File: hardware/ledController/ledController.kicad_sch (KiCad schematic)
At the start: 15 parts, among them IC1 PIC16F1769-I_ML, J1 Conn_01x06, J2 Screw_Terminal_01x02, J3 Screw_Terminal_01x02, J4 Conn_01x06, J5 Conn_01x03

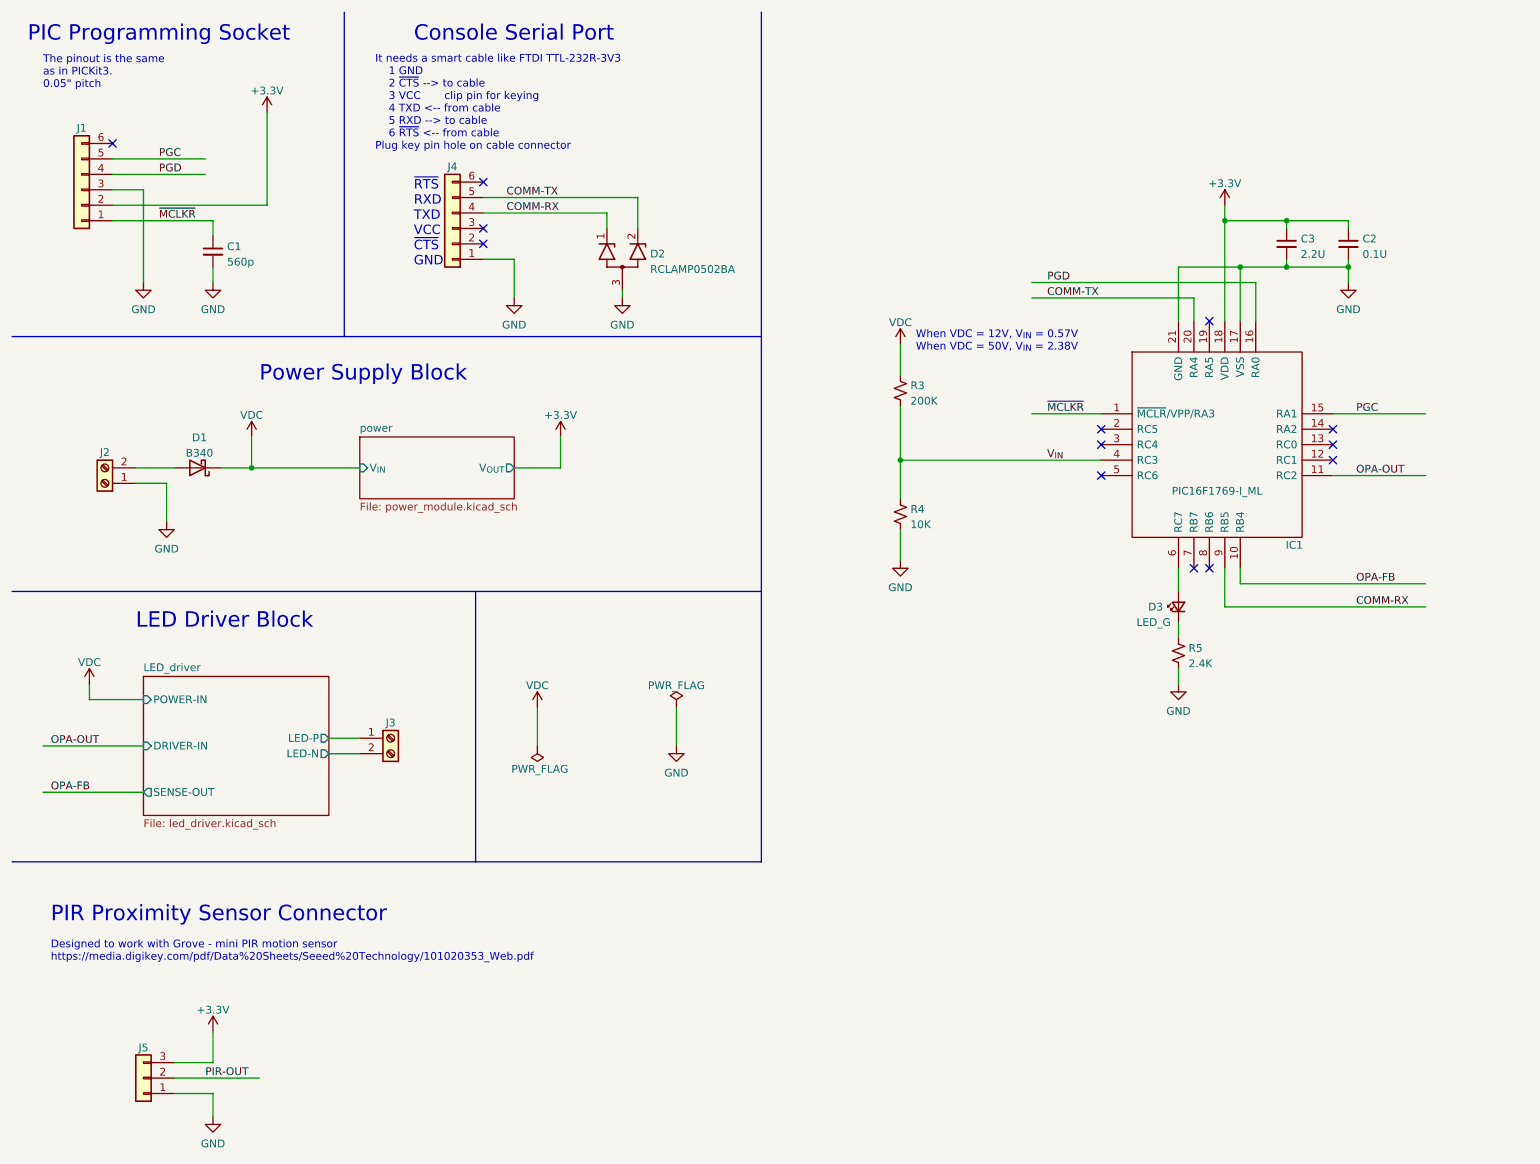
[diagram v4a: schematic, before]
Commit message: More schematic updates
Moved from PIR sensor to photoresistor + additional components
Added mounting holes
Moved to a stand alone 3.3V switcher
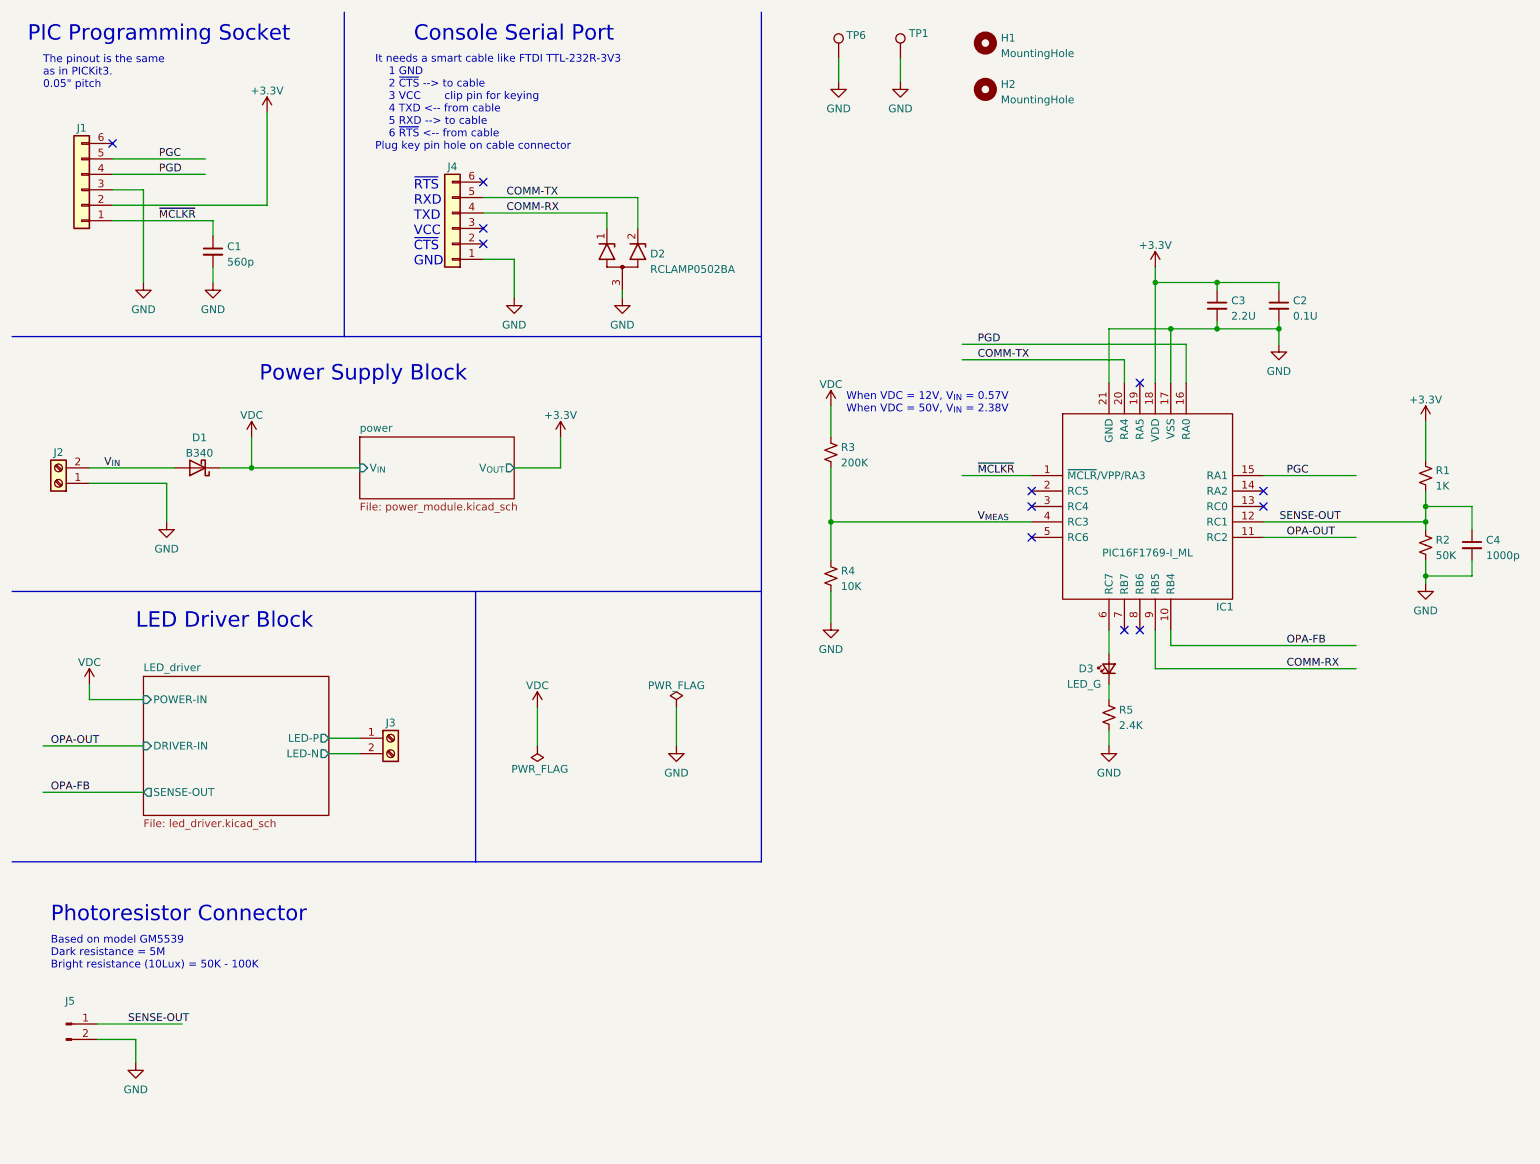
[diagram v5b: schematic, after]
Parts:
- removed J5: Conn_01x03, molex-footprints:353620350, symbol Connector_Generic:Conn_01x03
- added C4: 1000p, Capacitor_SMD:C_0402_1005Metric_Pad0.74x0.62mm_HandSolder, symbol Device:C_Small
- added H1, H2: MountingHole, MountingHole:MountingHole_2.5mm_Pad_TopBottom, symbol Mechanical:MountingHole
- added J5: Conn_01x02_Male, Connector_PinSocket_2.54mm:PinSocket_1x02_P2.54mm_Vertical, symbol Connector:Conn_01x02_Male
- added R1: 1K, Resistor_SMD:R_0603_1608Metric_Pad0.98x0.95mm_HandSolder, symbol Device:R_Small_US
- added R2: 50K, Resistor_SMD:R_0603_1608Metric_Pad0.98x0.95mm_HandSolder, symbol Device:R_Small_US
- added TP1, TP6: TestPoint, ym-footprints:TestPoint_Pad_0.185in_x_0.135in, symbol Connector:TestPoint
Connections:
- net +3.3V: now also R1.1
- net GND: now also C4.2, J5.2 (Pin_2), R2.2, TP1.1, TP6.1
- net V_{IN}: now also D1.2 (A), J2.2 (Pin_2); no longer IC1.4 (RC3), R3.2, R4.1
- net SENSE-OUT: now reaches IC1.12 (RC1)
- net SENSE-OUT: now also C4.1, J5.1 (Pin_1), R1.2, R2.1
- new net V_{MEAS}: IC1.4 (RC3), R3.2, R4.1
- no-connect marks 13 -> 12
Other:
- note added: "Based on model GM5539 Dark resistance = 5M Bright resistance (10Lux) = 50K - 100K"
- note added: "Photoresistor Connector"
- note removed: "Designed to work with Grove - mini PIR motion sensor https://media.digikey.com/pdf/Data%20Sheets/Seeed%20Technology/101020353_Web.pdf"
- note removed: "PIR Proximity Sensor Connector"
- moved on the sheet: C2, C3, D3, IC1, J2, R3, R4, R5

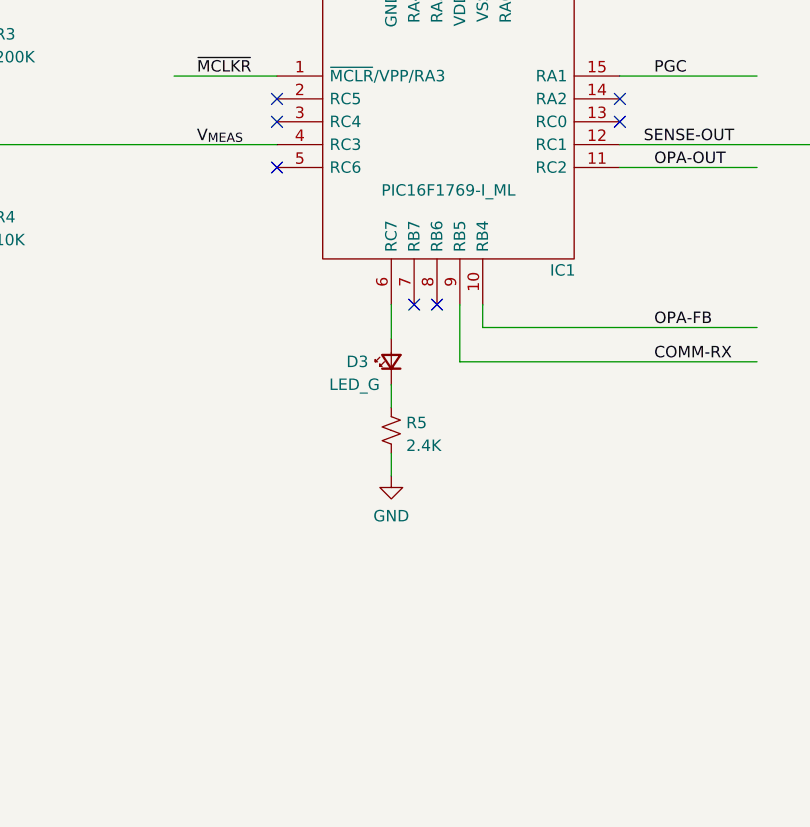
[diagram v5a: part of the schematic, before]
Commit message: Replaced debug LED
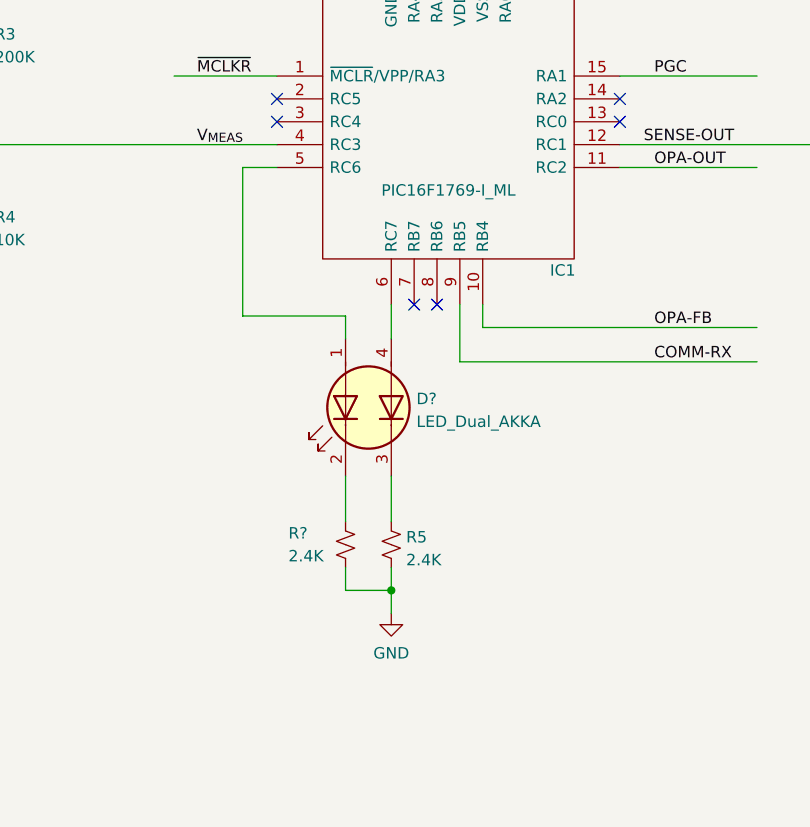
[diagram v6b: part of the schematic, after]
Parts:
- removed D3: LED_G, LED_SMD:LED_0805_2012Metric_Pad1.15x1.40mm_HandSolder, symbol Device:LED_Small
- added D?: LED_Dual_AKKA, LED_SMD:LED_Kingbright_APHBM2012_2x1.25mm, symbol Device:LED_Dual_AKKA
- added R?: 2.4K, Resistor_SMD:R_0603_1608Metric_Pad0.98x0.95mm_HandSolder, symbol Device:R_Small_US
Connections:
- net GND: now also R?.2
- net at IC1.5 (RC6): now also D?.1 (A1)
- net at IC1.6 (RC7): now also D?.4 (A2)
- net at R5.1: now also D?.3 (K2)
- new net: D?.2 (K1), R?.1
- no-connect marks 12 -> 11
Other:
- moved on the sheet: R5
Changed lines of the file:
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@@
   (junction (at 200.66 57.15) (diameter 0) (color 0 0 0 0)
+  )
+  (junction (at 193.04 146.05) (diameter 0) (color 0 0 0 0)
   )
   (junction (at 147.32 96.52) (diameter 0) (color 0 0 0 0)
@@
   (no_connect (at 90.17 48.26))
   (no_connect (at 90.17 40.64))
-  (no_connect (at 180.34 99.06))
   (no_connect (at 180.34 93.98))
   (no_connect (at 195.58 114.3))
@@
     (stroke (width 0) (type default) (color 0 0 0 0))
   )
+  (wire (pts (xy 193.04 114.3) (xy 193.04 118.11))
+    (stroke (width 0) (type default) (color 0 0 0 0))
+  )
   (wire (pts (xy 102.87 87.63) (xy 102.87 82.55))
     (stroke (width 0) (type default) (color 0 0 0 0))
@@
     (stroke (width 0) (type default) (color 0 0 0 0))
   )
+  (wire (pts (xy 176.53 99.06) (xy 176.53 115.57))
+    (stroke (width 0) (type default) (color 0 0 0 0))
+  )
   (wire (pts (xy 218.44 88.9) (xy 233.68 88.9))
     (stroke (width 0) (type default) (color 0 0 0 0))
   )
-  (wire (pts (xy 193.04 123.19) (xy 193.04 125.73))
-    (stroke (width 0) (type default) (color 0 0 0 0))
-  )
   (wire (pts (xy 52.07 87.63) (xy 69.85 87.63))
     (stroke (width 0) (type default) (color 0 0 0 0))
@@
     (stroke (width 0) (type default) (color 0 0 0 0))
   )
+  (wire (pts (xy 187.96 115.57) (xy 187.96 118.11))
+    (stroke (width 0) (type default) (color 0 0 0 0))
+  )
   (wire (pts (xy 218.44 96.52) (xy 245.11 96.52))
     (stroke (width 0) (type default) (color 0 0 0 0))
@@
     (stroke (width 0) (type default) (color 0 0 0 0))
   )
+  (wire (pts (xy 193.04 146.05) (xy 193.04 148.59))
+    (stroke (width 0) (type default) (color 0 0 0 0))
+  )
   (wire (pts (xy 90.17 53.34) (xy 95.25 53.34))
     (stroke (width 0) (type default) (color 0 0 0 0))
@@
     (stroke (width 0) (type default) (color 0 0 0 0))
   )
+  (wire (pts (xy 180.34 99.06) (xy 176.53 99.06))
+    (stroke (width 0) (type default) (color 0 0 0 0))
+  )
   (wire (pts (xy 245.11 93.98) (xy 252.73 93.98))
     (stroke (width 0) (type default) (color 0 0 0 0))
@@
     (stroke (width 0) (type default) (color 0 0 0 0))
   )
+  (wire (pts (xy 187.96 133.35) (xy 187.96 138.43))
+    (stroke (width 0) (type default) (color 0 0 0 0))
+  )
   (wire (pts (xy 25.4 90.17) (xy 38.1 90.17))
     (stroke (width 0) (type default) (color 0 0 0 0))
@@
     (stroke (width 0) (type default) (color 0 0 0 0))
   )
+  (wire (pts (xy 193.04 133.35) (xy 193.04 138.43))
+    (stroke (width 0) (type default) (color 0 0 0 0))
+  )
   (wire (pts (xy 245.11 96.52) (xy 245.11 97.79))
     (stroke (width 0) (type default) (color 0 0 0 0))
   )
+  (wire (pts (xy 187.96 143.51) (xy 187.96 146.05))
+    (stroke (width 0) (type default) (color 0 0 0 0))
+  )
   (wire (pts (xy 252.73 105.41) (xy 245.11 105.41))
     (stroke (width 0) (type default) (color 0 0 0 0))
@@
     (stroke (width 0) (type default) (color 0 0 0 0))
   )
-  (wire (pts (xy 193.04 130.81) (xy 193.04 133.35))
+  (wire (pts (xy 193.04 143.51) (xy 193.04 146.05))
     (stroke (width 0) (type default) (color 0 0 0 0))
   )
@@
     (stroke (width 0) (type default) (color 0 0 0 0))
   )
-  (wire (pts (xy 193.04 114.3) (xy 193.04 118.11))
-    (stroke (width 0) (type default) (color 0 0 0 0))
-  )
   (wire (pts (xy 252.73 102.87) (xy 252.73 105.41))
     (stroke (width 0) (type default) (color 0 0 0 0))
@@
     (stroke (width 0) (type default) (color 0 0 0 0))
   )
+  (wire (pts (xy 176.53 115.57) (xy 187.96 115.57))
+    (stroke (width 0) (type default) (color 0 0 0 0))
+  )
   (wire (pts (xy 95.25 87.63) (xy 102.87 87.63))
     (stroke (width 0) (type default) (color 0 0 0 0))
@@
   )
   (wire (pts (xy 26.67 181.61) (xy 33.02 181.61))
+    (stroke (width 0) (type default) (color 0 0 0 0))
+  )
+  (wire (pts (xy 187.96 146.05) (xy 193.04 146.05))
     (stroke (width 0) (type default) (color 0 0 0 0))
   )
@@
     (pin "2")
   )
+  (symbol (lib_id "Device:R_Small_US") (at 187.96 140.97 0) (unit 1)
+    (in_bom yes) (on_board yes)
+    (property "Reference" "R?" (id 0) (at 181.61 139.7 0)
+      (effects (font (size 1.27 1.27)) (justify left))
+    )
+    (property "Value" "2.4K" (id 1) (at 181.61 142.24 0)
+      (effects (font (size 1.27 1.27)) (justify left))
+    )
+    (property "Footprint" "Resistor_SMD:R_0603_1608Metric_Pad0.98x0.95mm_HandSolder" (id 2) (at 187.96 140.97 0)
+      (effects (font (size 1.27 1.27)) hide)
+    )
+    (property "Datasheet" "~" (id 3) (at 187.96 140.97 0)
+      (effects (font (size 1.27 1.27)) hide)
+    )
+    (pin "1")
+    (pin "2")
+  )
   (symbol (lib_id "power:GND") (at 220.98 67.31 0) (unit 1)
     (in_bom yes) (on_board yes) (fields_autoplaced)
@@
     (pin "1")
     (pin "2")
+  )
+  (symbol (lib_id "Device:LED_Dual_AKKA") (at 190.5 125.73 90) (mirror x) (unit 1)
+    (in_bom yes) (on_board yes) (fields_autoplaced)
+    (property "Reference" "D?" (id 0) (at 195.834 124.7683 90)
+      (effects (font (size 1.27 1.27)) (justify right))
+    )
+    (property "Value" "LED_Dual_AKKA" (id 1) (at 195.834 127.3052 90)
+      (effects (font (size 1.27 1.27)) (justify right))
+    )
+    (property "Footprint" "LED_SMD:LED_Kingbright_APHBM2012_2x1.25mm" (id 2) (at 190.5 126.492 0)
+      (effects (font (size 1.27 1.27)) hide)
+    )
+    (property "Datasheet" "~" (id 3) (at 190.5 126.492 0)
+      (effects (font (size 1.27 1.27)) hide)
+    )
+    (pin "1")
+    (pin "2")
+    (pin "3")
+    (pin "4")
   )
   (symbol (lib_id "power:VDC") (at 25.4 123.19 0) (unit 1)
@@
     (pin "6")
   )
-  (symbol (lib_id "Device:R_Small_US") (at 193.04 128.27 0) (unit 1)
-    (in_bom yes) (on_board yes) (fields_autoplaced)
-    (property "Reference" "R5" (id 0) (at 194.691 127.4353 0)
-      (effects (font (size 1.27 1.27)) (justify left))
-    )
-    (property "Value" "2.4K" (id 1) (at 194.691 129.9722 0)
-      (effects (font (size 1.27 1.27)) (justify left))
-    )
-    (property "Footprint" "Resistor_SMD:R_0603_1608Metric_Pad0.98x0.95mm_HandSolder" (id 2) (at 193.04 128.27 0)
-      (effects (font (size 1.27 1.27)) hide)
-    )
-    (property "Datasheet" "~" (id 3) (at 193.04 128.27 0)
+  (symbol (lib_id "Device:R_Small_US") (at 193.04 140.97 0) (unit 1)
+    (in_bom yes) (on_board yes) (fields_autoplaced)
+    (property "Reference" "R5" (id 0) (at 194.691 140.1353 0)
+      (effects (font (size 1.27 1.27)) (justify left))
+    )
+    (property "Value" "2.4K" (id 1) (at 194.691 142.6722 0)
+      (effects (font (size 1.27 1.27)) (justify left))
+    )
+    (property "Footprint" "Resistor_SMD:R_0603_1608Metric_Pad0.98x0.95mm_HandSolder" (id 2) (at 193.04 140.97 0)
+      (effects (font (size 1.27 1.27)) hide)
+    )
+    (property "Datasheet" "~" (id 3) (at 193.04 140.97 0)
       (effects (font (size 1.27 1.27)) hide)
     )
@@
     (pin "2")
   )
-  (symbol (lib_id "power:GND") (at 193.04 133.35 0) (unit 1)
-    (in_bom yes) (on_board yes) (fields_autoplaced)
-    (property "Reference" "#PWR015" (id 0) (at 193.04 139.7 0)
-      (effects (font (size 1.27 1.27)) hide)
-    )
-    (property "Value" "GND" (id 1) (at 193.04 137.7934 0))
-    (property "Footprint" "" (id 2) (at 193.04 133.35 0)
-      (effects (font (size 1.27 1.27)) hide)
-    )
-    (property "Datasheet" "" (id 3) (at 193.04 133.35 0)
+  (symbol (lib_id "power:GND") (at 193.04 148.59 0) (unit 1)
+    (in_bom yes) (on_board yes) (fields_autoplaced)
+    (property "Reference" "#PWR015" (id 0) (at 193.04 154.94 0)
+      (effects (font (size 1.27 1.27)) hide)
+    )
+    (property "Value" "GND" (id 1) (at 193.04 153.0334 0))
+    (property "Footprint" "" (id 2) (at 193.04 148.59 0)
+      (effects (font (size 1.27 1.27)) hide)
+    )
+    (property "Datasheet" "" (id 3) (at 193.04 148.59 0)
       (effects (font (size 1.27 1.27)) hide)
     )
@@
     )
     (property "Datasheet" "~" (id 3) (at 245.11 100.33 0)
-      (effects (font (size 1.27 1.27)) hide)
-    )
-    (pin "1")
-    (pin "2")
-  )
-  (symbol (lib_id "Device:LED_Small") (at 193.04 120.65 90) (unit 1)
-    (in_bom yes) (on_board yes)
-    (property "Reference" "D3" (id 0) (at 190.5 120.65 90)
-      (effects (font (size 1.27 1.27)) (justify left))
-    )
-    (property "Value" "LED_G" (id 1) (at 191.77 123.19 90)
-      (effects (font (size 1.27 1.27)) (justify left))
-    )
-    (property "Footprint" "LED_SMD:LED_0805_2012Metric_Pad1.15x1.40mm_HandSolder" (id 2) (at 193.04 120.65 90)
-      (effects (font (size 1.27 1.27)) hide)
-    )
-    (property "Datasheet" "~" (id 3) (at 193.04 120.65 90)
       (effects (font (size 1.27 1.27)) hide)
     )
@@
       (reference "D2") (unit 1) (value "RCLAMP0502BA") (footprint "Package_TO_SOT_SMD:SOT-523")
     )
-    (path "/f107034a-03b5-49af-be3c-d6a84a8f1eb8"
-      (reference "D3") (unit 1) (value "LED_G") (footprint "LED_SMD:LED_0805_2012Metric_Pad1.15x1.40mm_HandSolder")
+    (path "/66c50902-9d0c-447a-90de-d45899b9f06c"
+      (reference "D?") (unit 1) (value "LED_Dual_AKKA") (footprint "LED_SMD:LED_Kingbright_APHBM2012_2x1.25mm")
     )
     (path "/31243e06-0979-4fae-860f-4cad80206009"
@@
     )
     (path "/3bc33efb-21fe-4c44-a8f6-d39938b6f203/b65c1875-b5c3-4cae-8f5d-c778cfe9d0eb"
-      (reference "R9") (unit 1) (value "1") (footprint "Resistor_SMD:R_1210_3225Metric_Pad1.30x2.65mm_HandSolder")
+      (reference "R9") (unit 1) (value "1") (footprint "Resistor_SMD:R_1206_3216Metric_Pad1.30x1.75mm_HandSolder")
     )
     (path "/3bc33efb-21fe-4c44-a8f6-d39938b6f203/a3a6bb23-5ba8-4d09-96fb-cbf7fb2f8f1c"
-      (reference "R10") (unit 1) (value "1") (footprint "Resistor_SMD:R_1210_3225Metric_Pad1.30x2.65mm_HandSolder")
+      (reference "R10") (unit 1) (value "1") (footprint "Resistor_SMD:R_1206_3216Metric_Pad1.30x1.75mm_HandSolder")
+    )
+    (path "/3c0907ef-a933-4de9-8705-d6d11137d646"
+      (reference "R?") (unit 1) (value "2.4K") (footprint "Resistor_SMD:R_0603_1608Metric_Pad0.98x0.95mm_HandSolder")
     )
     (path "/04b0a461-f9a3-4e36-bb78-ad096b231c16"
